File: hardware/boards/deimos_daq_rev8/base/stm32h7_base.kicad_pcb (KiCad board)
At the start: 4 copper layers, 197 parts, among them IC1 STM32H743ZIT6, IC10001 TPS560430XDBVR, IC10002 TPS560430XDBVR, IC4001 TPS560430XDBVR, IC5004 REF35102QDBVR, IC8001 INA826AIDR, J3001 RCH_RC01133, J4 Conn_02x07_Odd_Even, J8001 Barrel_Jack PJ-202BH, T1 H1102NLT, U2001 NTJD4001NT1G, U4001 INA181A2, U5 LAN8742A, U6002 ADR4525, Y1 SiT1602BI-21-33S-48.000000, Y2 NX2016SA-25.000M-STD-CZS-1

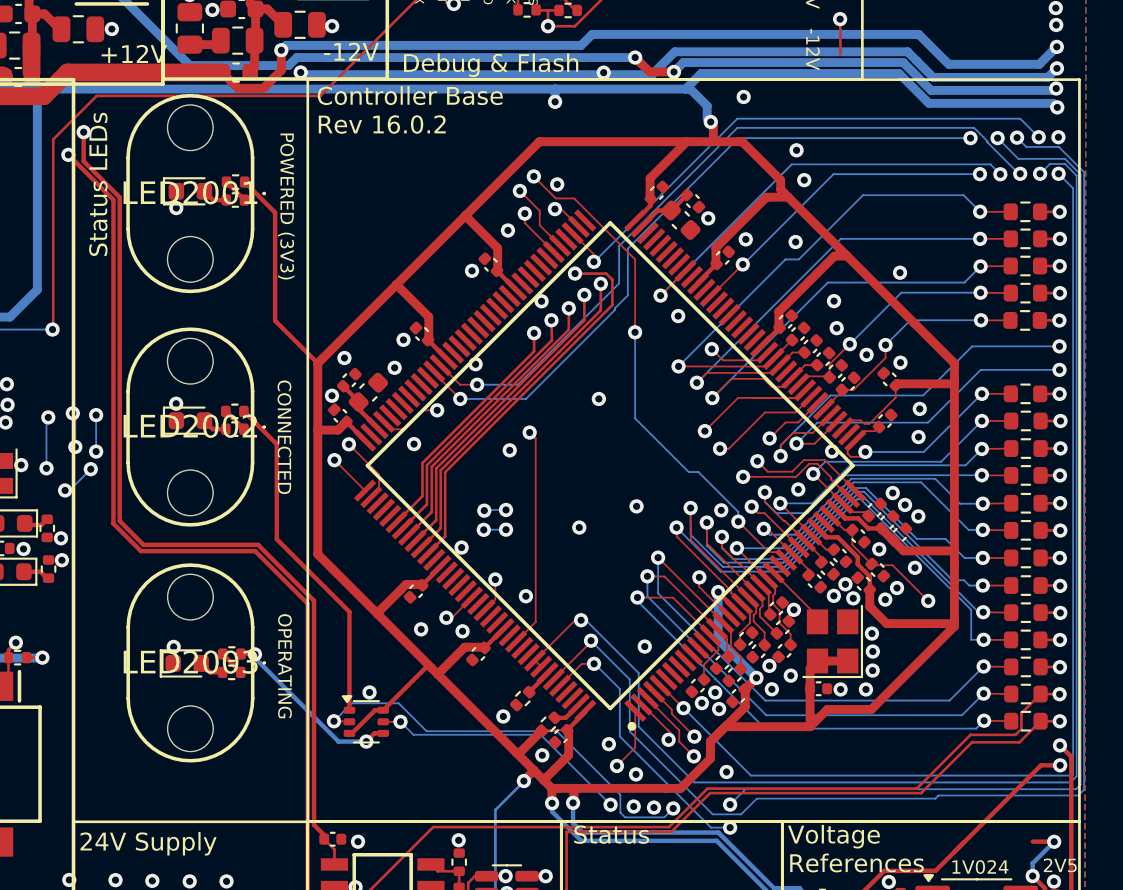
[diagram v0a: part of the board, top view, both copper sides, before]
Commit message: update base module layout
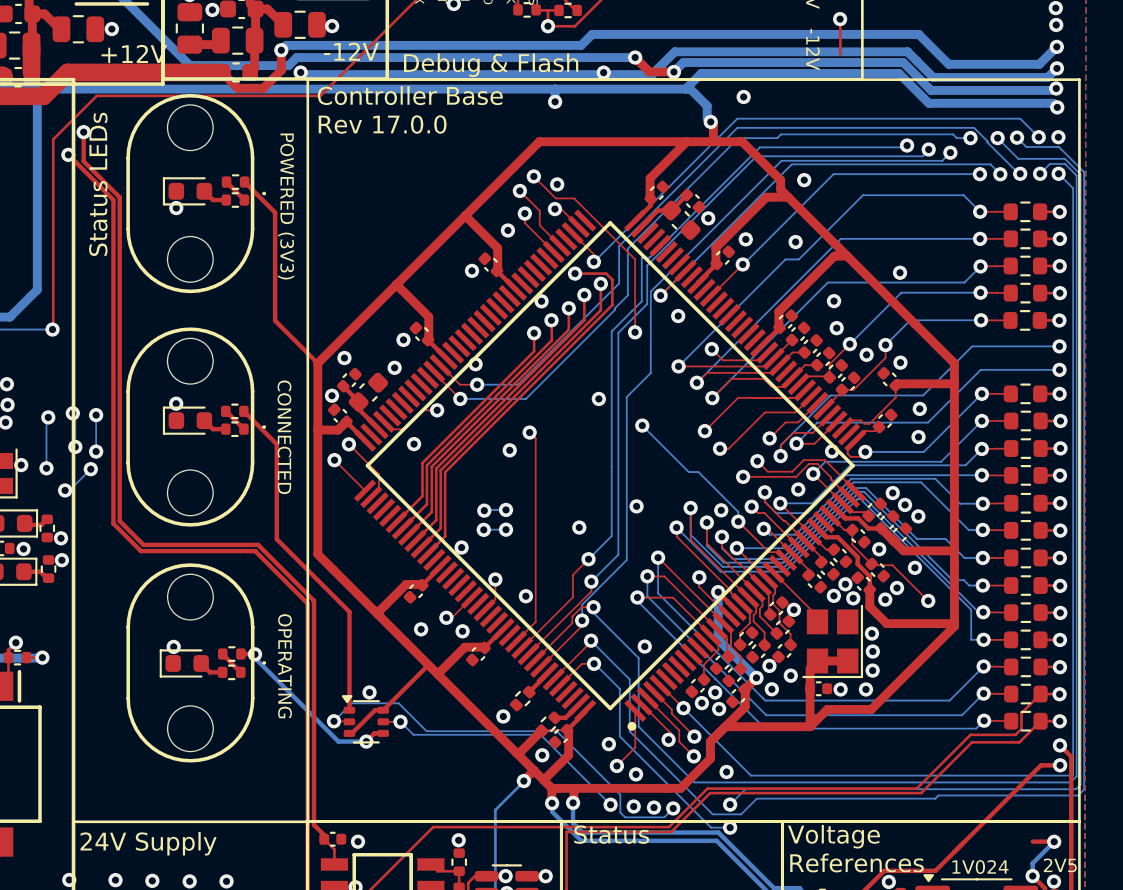
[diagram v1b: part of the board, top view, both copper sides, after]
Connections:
- net /COUNTER0 renamed /ENCODER1_A
- net /ENCODER0_0 renamed /ENCODER0_A
- net /ENCODER0_1 renamed /ENCODER0_B
- IC1 pad 134: unconnected-(IC1-PB4-Pad134) -> /ENCODER3_A
- IC1 pad 135: unconnected-(IC1-PB5-Pad135) -> /ENCODER3_B
- IC1 pad 136: /FREQ0 -> /ENCODER2_A
- IC1 pad 137: /FREQ0 -> /ENCODER2_B
- IC1 pad 5: /FREQ1 -> /PWM0
- IC1 pad 97: /PWM0 -> /ENCODER1_B
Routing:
- net /ENCODER2_A: track 0.00 -> 74.9 mm, vias 0 -> 2
- net /FREQ0: track 73.9 -> 0.00 mm, vias 2 -> 0
- net /FREQ1: track 59.4 -> 0.00 mm, vias 2 -> 0
- net /ENCODER1_B: track 0.00 -> 44.2 mm, vias 0 -> 3
- net /ENCODER2_B: track 0.00 -> 43.7 mm, vias 0 -> 2
- net /ENCODER3_B: track 0.00 -> 43.2 mm, vias 0 -> 2
- net /ENCODER3_A: track 0.00 -> 42.3 mm, vias 0 -> 2
- net /PWM0: track 44.0 -> 59.4 mm, vias 3 -> 2
- net GND: vias 139 -> 138
- net /Micro/DEBUG_RESET: vias 7 -> 8
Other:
- board text added: "Controller Base Rev 17.0.0"
- board text removed: "Controller Base Rev 16.0.2"

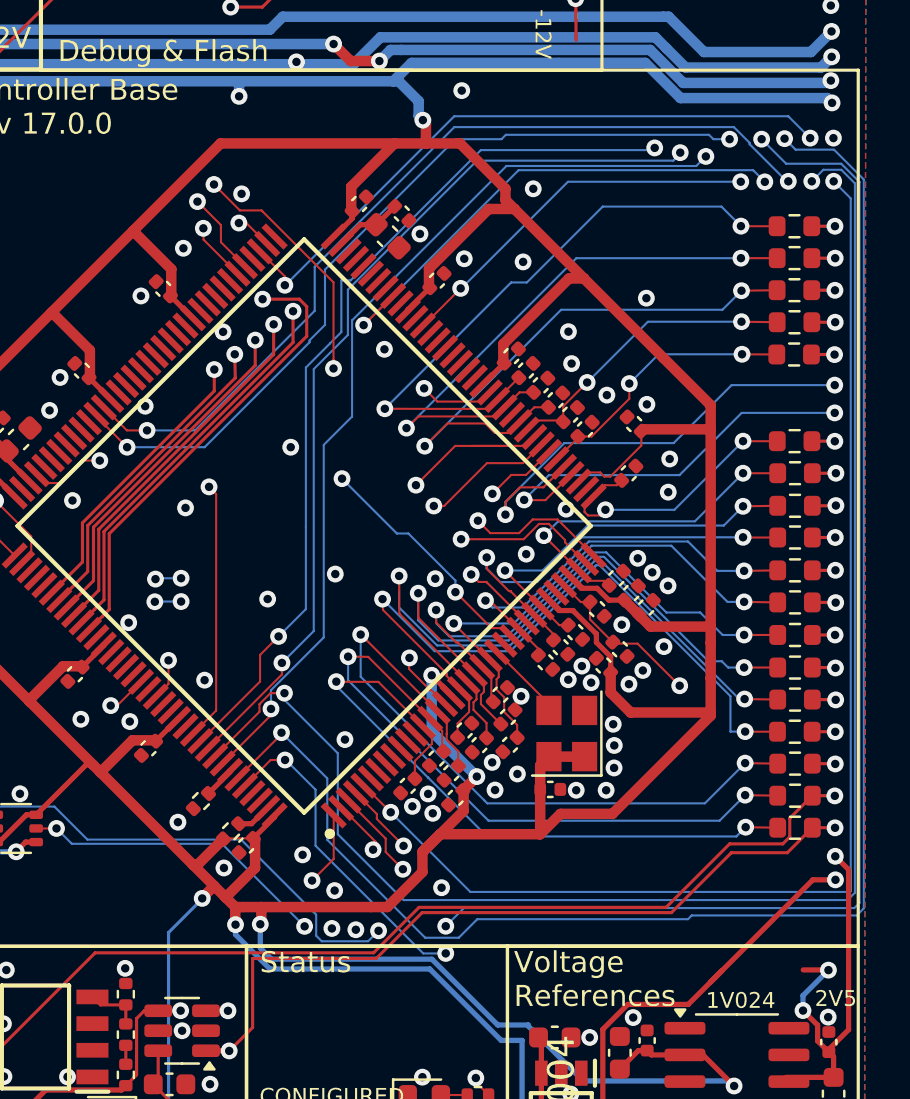
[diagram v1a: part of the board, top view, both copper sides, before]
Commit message: finish layout and generate fab files
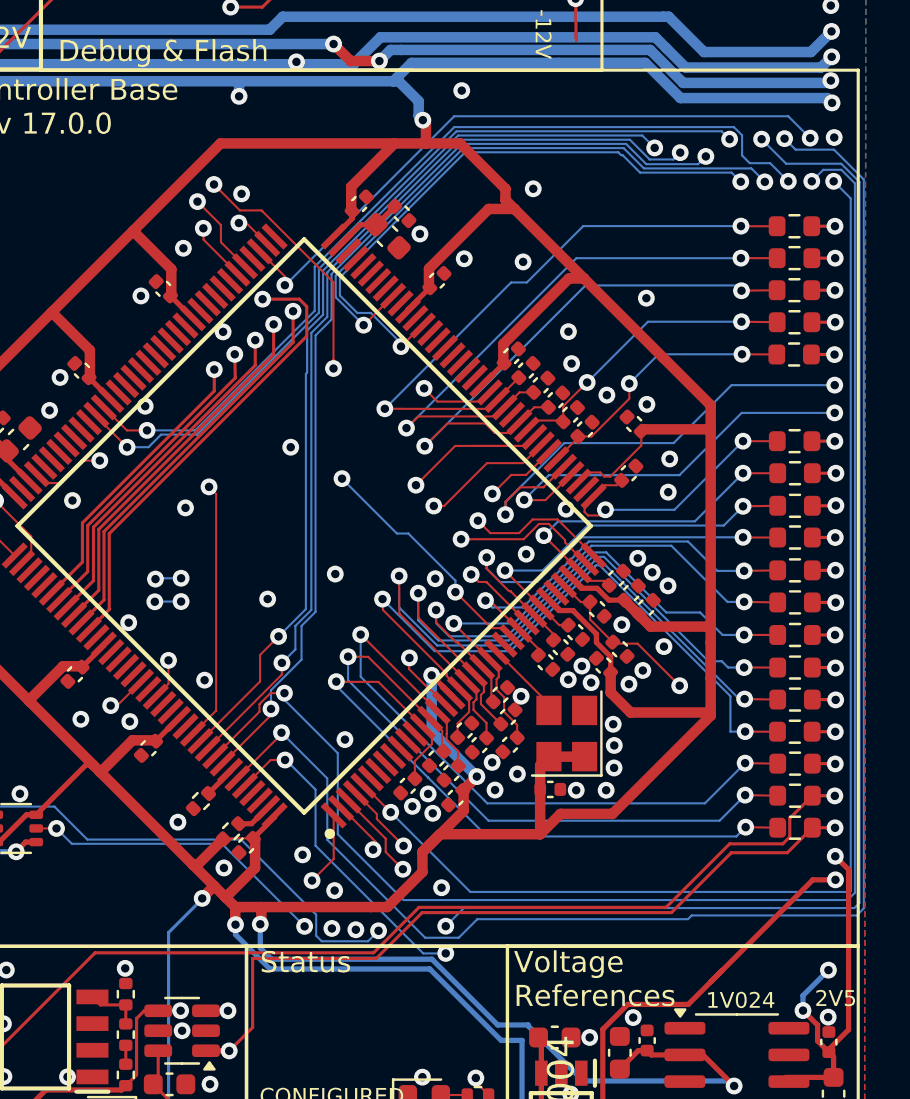
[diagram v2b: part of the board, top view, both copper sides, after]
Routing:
- net /ENCODER0_A: track 18.0 -> 28.5 mm
- net /ENCODER1_B: track 44.2 -> 38.5 mm, vias 3 -> 2
- net /ENCODER0_B: track 24.4 -> 28.5 mm
- net /ENCODER2_B: track 43.7 -> 46.4 mm
- net /PWM0: track 59.4 -> 61.5 mm, vias 2 -> 3
- net /ENCODER3_B: track 43.2 -> 45.0 mm
- net /ENCODER3_A: track 42.3 -> 43.6 mm
- net +2V5: track 41.6 -> 40.4 mm
- net /Micro/AIN19_Filt: track 30.1 -> 29.4 mm
- net /ENCODER1_A: track 41.4 -> 41.9 mm
- net GND: vias 138 -> 137

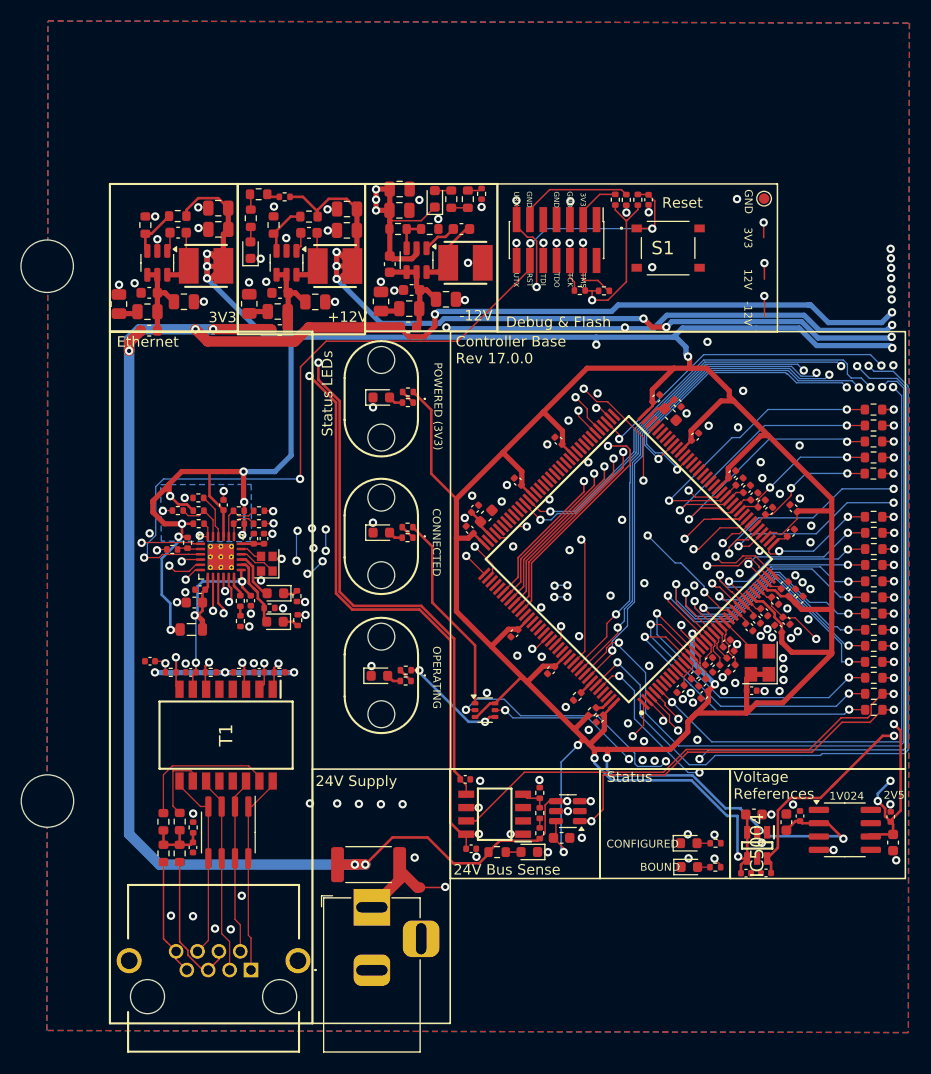
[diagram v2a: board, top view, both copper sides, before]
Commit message: put testpoints back in and generate fab files again
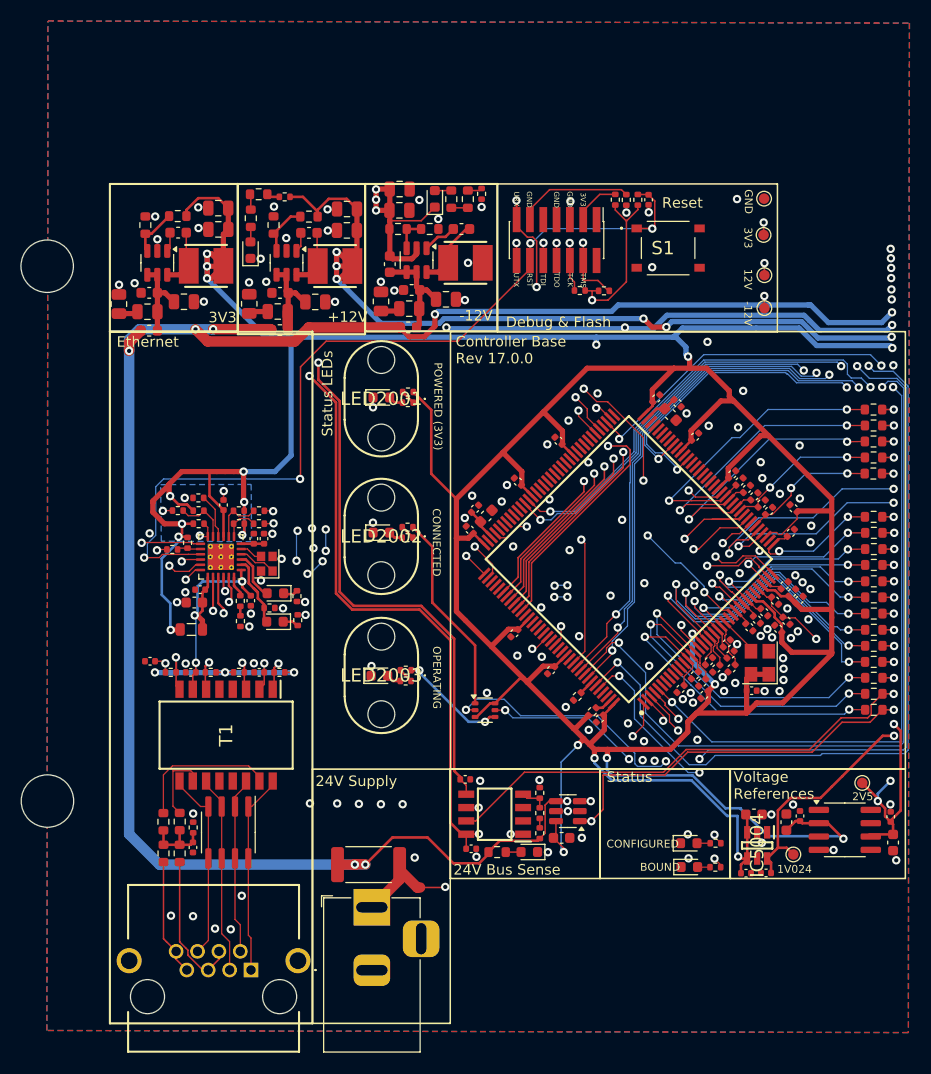
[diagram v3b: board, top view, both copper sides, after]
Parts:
- added TP10001: TestPoint_+12V, TestPoint:TestPoint_Pad_D1.0mm, F.Cu at (103.3, 79.2)
- added TP10003: TestPoint_+2V5, TestPoint:TestPoint_Pad_D1.0mm, F.Cu at (112.6, 127.7)
- added TP10004: TestPoint_+3V3, TestPoint:TestPoint_Pad_D1.0mm, F.Cu at (103.2, 75.4)
- added TP10005: TestPoint_+1V024, TestPoint:TestPoint_Pad_D1.0mm, F.Cu at (106.0, 134.5)
- added TP11001: TestPoint_+12V, TestPoint:TestPoint_Pad_D1.0mm, F.Cu at (103.3, 82.4)
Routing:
- net +2V5: track 40.4 -> 42.8 mm
- net +1V024: track 21.3 -> 22.3 mm
- net -12V: track 159.6 -> 158.8 mm
